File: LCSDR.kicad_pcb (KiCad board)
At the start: 2 copper layers, 100 x 95 mm, 92 parts, among them CON1 AVR-ISP-6, J1 USB_B_Mini, J10 Conn_01x01, J11 Conn_01x01, J12 Conn_01x10, J13 Jack-DC, J14 Conn_01x04, J16 UART, J2 Power, J3 Conn_01x10, J4 Conn_01x10, J5 USB_OTG, J6 Power, J7 Conn_01x10, J8 Conn_01x01, J9 Conn_01x01, Q1 MMBT2907LT1G, Q2 Q_NPN_BEC, U1 LD1117S33TR, U10 LD1117S33CTR, U11 ATMEGA8-16AU, U2 PCM2900C, U3 PCA9306, U4 Si570, U5 MC34063, U6 LD1117S33CTR, U7 78M09, U8 LD1117S33CTR, Y1 20Mhz, Y2 12Mhz

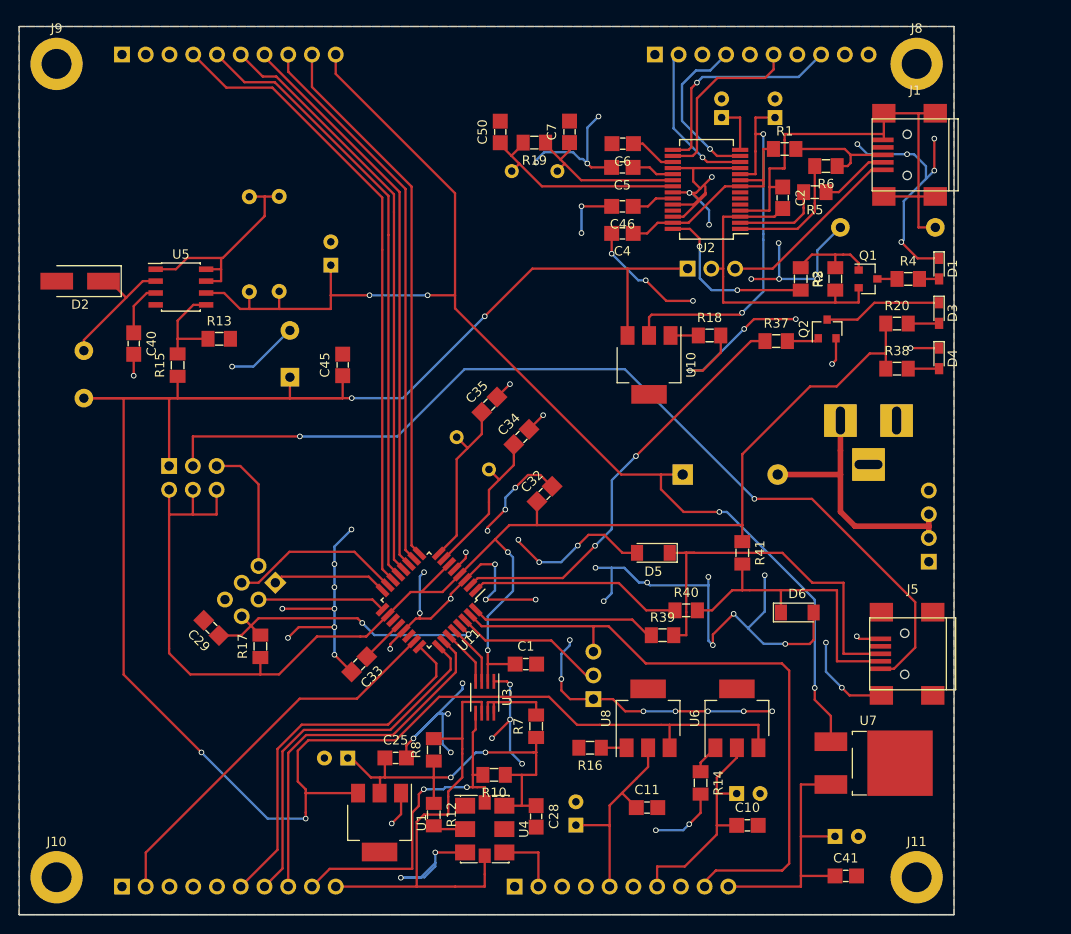
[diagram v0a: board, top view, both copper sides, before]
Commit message: delete microSD
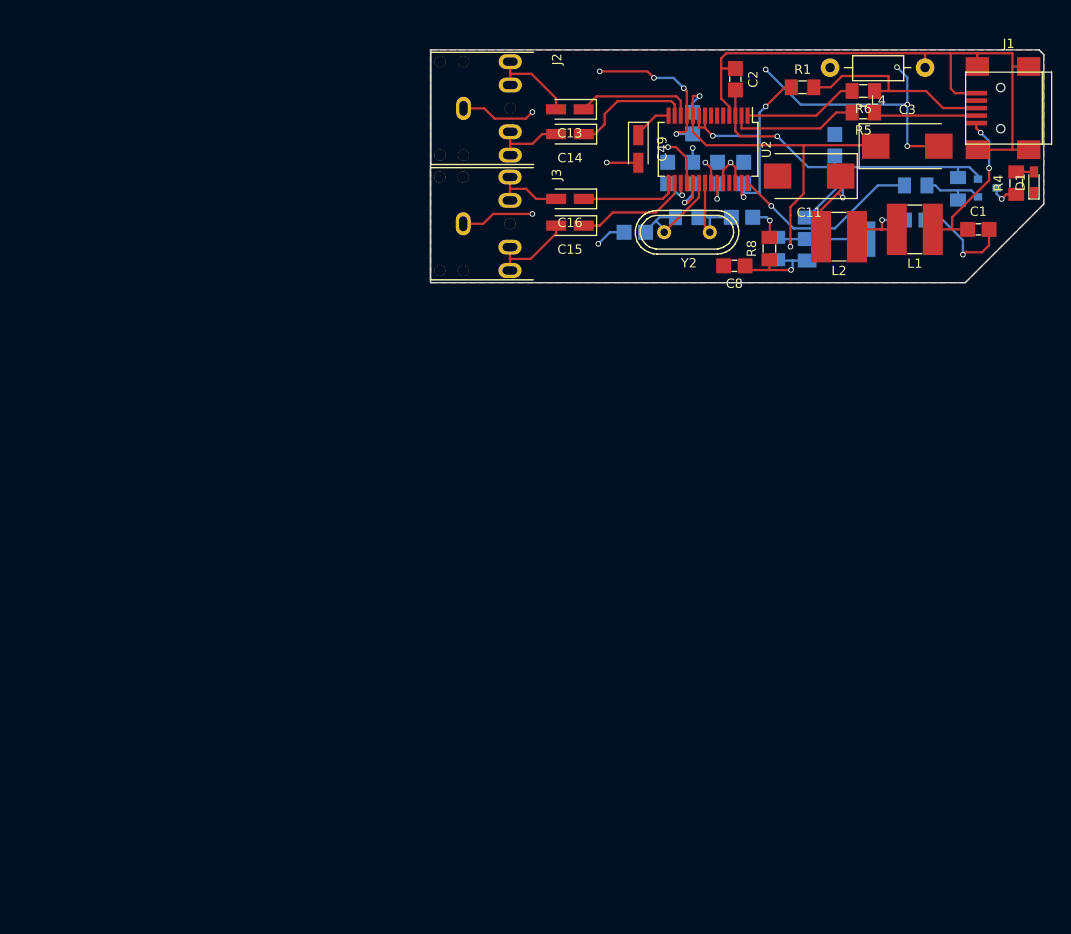
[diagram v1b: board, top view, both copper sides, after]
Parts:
- removed C25, C28, C29, C32, C33, C41, C45: 100nF, UI:C_1206_0603
- removed C26, C44: 100uF, Capacitors_THT:CP_Radial_D6.3mm_P2.50mm
- removed C34, C35: 22pF, UI:C_1206_0603
- removed C36: 10uF, Capacitors_THT:CP_Radial_D6.3mm_P2.50mm
- removed C38: 1000uF, Capacitors_ThroughHole:CP_Radial_D10.0mm_P5.00mm
- removed C40: 180pF, UI:C_1206_0603
- removed CON1: AVR-ISP-6, Pin_Headers:Pin_Header_Straight_2x03_Pitch2.54mm
- removed D2: SS14, Diodes_SMD:D_SMA_Handsoldering
- removed D3, D4: LED_Small, LEDs:LED_0603_HandSoldering
- removed D5, D6: 3.3V, Diodes_SMD:D_MiniMELF
- removed D7: SS14, Diodes_THT:D_DO-41_SOD81_P10.16mm_Horizontal
- removed J10, J11, J8, J9: Conn_01x01, Mounting_Holes:MountingHole_3.2mm_M3_DIN965_Pad
- removed J12, J4, J7: Conn_01x10, Pin_Headers:Pin_Header_Straight_1x10_Pitch2.54mm
- removed J13: Jack-DC, Connectors:BARREL_JACK
- removed J14: Conn_01x04, Pin_Headers:Pin_Header_Straight_1x04_Pitch2.54mm
- removed J16: UART, Pin_Headers:Pin_Header_Straight_1x03_Pitch2.54mm
- removed J5: USB_OTG, Connectors:USB_Mini-B
- removed J6: Power, Pin_Headers:Pin_Header_Straight_2x03_Pitch2.54mm
- removed Q2: Q_NPN_BEC, TO_SOT_Packages_SMD:SOT-23
- removed R10: 4.7k, UI:R_1206_0603
- removed R11, R9: 0.49R, Resistors_ThroughHole:R_Axial_DIN0207_L6.3mm_D2.5mm_P10.16mm_Horizontal
- removed R12, R17: 10k, UI:R_1206_0603
- removed R13: 11k, UI:R_1206_0603
- removed R14, R16: 91R, UI:R_1206_0603
- removed R15: 18k, UI:R_1206_0603
- removed R18: 22R, UI:R_1206_0603
- removed R20: 680R, UI:R_1206_0603
- removed R37: 2.2k, UI:R_1206_0603
- removed R38, R39, R40: 68R, UI:R_1206_0603
- removed R41: 1.5k, UI:R_1206_0603
- removed U10, U6, U8: LD1117S33CTR, SOT-223
- removed U11: ATMEGA8-16AU, Housings_QFP:TQFP-32_7x7mm_Pitch0.8mm
- removed U3: PCA9306, Housings_SSOP:SSOP-8_2.95x2.8mm_Pitch0.65mm
- removed U4: Si570, Oscillators:Oscillator_SMD_SI570_SI571_Standard
- removed U5: MC34063, UI:SOIC-8_3.9x4.9mm_Pitch1.27mm
- removed U7: 78M09, TO_SOT_Packages_SMD:TO-252-2_Rectifier
- removed Y1: 20Mhz, UI:Crystal_HC49-U_Vertical
- added C12: 100nF, UI:C_1206_0603, B.Cu at (187.0, 50.3)
- added C13: 2.2µF, Capacitors_Tantalum_SMD:CP_Tantalum_Case-A_EIA-3216-18_Wave, F.Cu at (173.9, 48.9)
- added C14: 2.2µF, Capacitors_Tantalum_SMD:CP_Tantalum_Case-A_EIA-3216-18_Wave, F.Cu at (173.9, 51.5)
- added C15: 2.2µF, Capacitors_Tantalum_SMD:CP_Tantalum_Case-A_EIA-3216-18_Wave, F.Cu at (173.9, 61.3)
- added C16: 2.2µF, Capacitors_Tantalum_SMD:CP_Tantalum_Case-A_EIA-3216-18_Wave, F.Cu at (173.9, 58.4)
- added L1: 4.7µH, UI:Choke_CD54, F.Cu at (210.8, 61.7)
- C10, C50, C7, Q1, R19, R2, R3: moved to B.Cu
- C11: value 100nF -> 100µF; footprint UI:C_1206_0603 -> Capacitors_Tantalum_SMD:CP_Tantalum_Case-D_EIA-7343-31_Wave
- C3: value 10uF -> 47uF; footprint Capacitors_THT:CP_Radial_D5.0mm_P2.00mm -> Capacitors_Tantalum_SMD:CP_Tantalum_Case-D_EIA-7343-31_Wave; moved to F.Cu
- C4, C46, C5, C6: value 100nF -> 1uF; moved to B.Cu
- C49: footprint Capacitors_THT:CP_Radial_D5.0mm_P2.00mm -> Capacitors_Tantalum_SMD:CP_Tantalum_Case-A_EIA-3216-18_Wave; moved to F.Cu
- C8: value 100uF -> 100nF; footprint Capacitors_THT:CP_Radial_D6.3mm_P2.50mm -> UI:C_1206_0603; moved to F.Cu
- C9: value 100uF -> 100nF; footprint Capacitors_THT:CP_Radial_D6.3mm_P2.50mm -> UI:C_1206_0603
- J2: value Power -> IN; footprint Pin_Headers:Pin_Header_Straight_1x03_Pitch2.54mm -> UI:audio_jack_3_5mm_PJ307; moved to F.Cu
- J3: value Conn_01x10 -> OUT; footprint Pin_Headers:Pin_Header_Straight_1x10_Pitch2.54mm -> UI:audio_jack_3_5mm_PJ307; moved to F.Cu
- L2: value 100uH -> 4.7µH; footprint Choke_Toroid_ThroughHole:Choke_Toroid_5x10mm_Vertical -> UI:Choke_CD54; moved to F.Cu
- L4, Y2: moved to F.Cu
- R7: value 200k -> 150R; moved to B.Cu
- R8: value 4.7k -> 300R
- U1: value LD1117S33TR -> LM317_3PinPackage; footprint SOT-223 -> TO_SOT_Packages_SMD:SOT-223-3_TabPin2; moved to B.Cu
- moved L2 86.7 mm to (202.7, 62.5), turned to 180 degrees
- moved U1 79.3 mm to (202.4, 62.7), turned to 0 degrees
- moved C9 74.2 mm to (210.8, 60.7), turned to 0 degrees
- moved C10 73.3 mm to (202.2, 52.7), turned to 90 degrees
- moved C11 69.7 mm to (199.5, 56.0), turned to 180 degrees
- moved C1 67.1 mm to (217.6, 61.7)
- moved R8 64.5 mm to (195.2, 63.8)
- moved R7 57.2 mm to (196.1, 63.8), turned to 270 degrees
- moved C8 56.5 mm to (191.5, 65.6), turned to 180 degrees
- moved J2 29.5 mm to (162.5, 48.8), turned to 90 degrees
- moved C50 27.4 mm to (192.3, 60.4), turned to 0 degrees
- moved J3 27.3 mm to (162.5, 61.1), turned to 90 degrees
- moved R19 18.1 mm to (186.4, 60.4), turned to 0 degrees
- moved Y2 17.6 mm to (186.4, 62.0), turned to 0 degrees
- moved L4 17.1 mm to (206.9, 44.4)
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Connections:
- C1 pad 1: +5VD -> Net-(C1-Pad1)
- C10 pad 1: MIXER -> Net-(C10-Pad1)
- C11 pad 1: ROTATOR -> Net-(C10-Pad1)
- C2 pad 2: Net-(C2-Pad2) -> Net-(C10-Pad1)
- C3 pad 1: Net-(C3-Pad1) -> Net-(C12-Pad1)
- C8 pad 1: MIXER -> Net-(C8-Pad1)
- C9 pad 1: ROTATOR -> Net-(C9-Pad1)
- J1 pad 1: Net-(J1-Pad1) -> Net-(C1-Pad1)
- J2 pad 1: +5V -> Net-(C14-Pad2)
- J2 pad 2: Net-(C2-Pad2) -> Net-(C13-Pad2)
- J2 pad 3: Net-(J1-Pad1) -> GND
- J3 pad 1: GND -> Net-(C15-Pad2)
- J3 pad 2: LINE_IN_LEFT -> Net-(C16-Pad2)
- J3 pad 4: LINE_IN_RIGHT -> Net-(C15-Pad2)
- J3 pad 5: GND -> Net-(C16-Pad2)
- J3 pad 6: LINE_OUT_LEFT -> (no net)
- J3 pad 7: GND -> (no net)
- J3 pad 8: LINE_OUT_RIGHT -> (no net)
- J3 pad 9: GND -> (no net)
- L2 pad 1: Net-(D2-Pad1) -> Net-(C9-Pad1)
- L2 pad 2: +5V -> Net-(C10-Pad1)
- Q1 pad 2: Net-(C2-Pad2) -> Net-(C10-Pad1)
- R2 pad 1: Net-(C2-Pad2) -> Net-(C10-Pad1)
- R7 pad 1: Net-(C25-Pad1) -> Net-(C12-Pad1)
- R7 pad 2: Net-(R7-Pad2) -> Net-(C8-Pad1)
- R8 pad 1: Net-(C25-Pad1) -> Net-(C8-Pad1)
- R8 pad 2: I2C_SCL -> GND
- U1 pad 1: GND -> Net-(C8-Pad1)
- U1 pad 2: Net-(C25-Pad1) -> Net-(C12-Pad1)
- U1 pad 3: +5V -> Net-(C10-Pad1)
- U2 pad 10: Net-(C3-Pad1) -> Net-(C12-Pad1)
- U2 pad 12: LINE_IN_LEFT -> Net-(C13-Pad1)
- U2 pad 13: LINE_IN_RIGHT -> Net-(C14-Pad1)
- U2 pad 15: LINE_OUT_RIGHT -> Net-(C16-Pad1)
- U2 pad 16: LINE_OUT_LEFT -> Net-(C15-Pad1)
- U2 pad 3: Net-(C2-Pad2) -> Net-(C10-Pad1)
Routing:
- net GND: track 383.0 -> 98.2 mm, vias 82 -> 18
- net +5V: track 245.8 -> 0.00 mm, vias 4 -> 0
- net +5VD: track 159.9 -> 0.00 mm, vias 2 -> 0
- net +12V: track 138.7 -> 0.00 mm, vias 4 -> 0
- net Net-(J5-Pad1): track 103.3 -> 0.00 mm, vias 2 -> 0
- net IF_RX_TX: track 70.3 -> 0.00 mm
- net IO0: track 67.9 -> 0.00 mm
- net IO1: track 65.6 -> 0.00 mm
- net IO2: track 63.1 -> 0.00 mm
- net IO3: track 60.9 -> 0.00 mm
- net S1_RX_TX: track 59.5 -> 0.00 mm
- net S2_RX_TX: track 58.1 -> 0.00 mm
- net Net-(C10-Pad1): track 0.00 -> 53.2 mm, vias 0 -> 2
- net Net-(C12-Pad1): track 0.00 -> 48.9 mm, vias 0 -> 2
- net I2C_SCL: track 48.9 -> 0.00 mm
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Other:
- board size 100 x 95 mm -> 65.6 x 24.9 mm
